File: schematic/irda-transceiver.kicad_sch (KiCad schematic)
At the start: 27 parts, among them J1 Conn_01x03_Pin, J2 Conn_01x03_Pin, J3 Conn_01x03_Pin, J4 Conn_01x03_Pin, J5 Conn_01x03_Pin, J6 Conn_01x03_Pin, J7 Conn_01x06_Pin, U1 MCP2120-I/P, U2 TFDU4101-TT3, Y1 7.3728 MHz

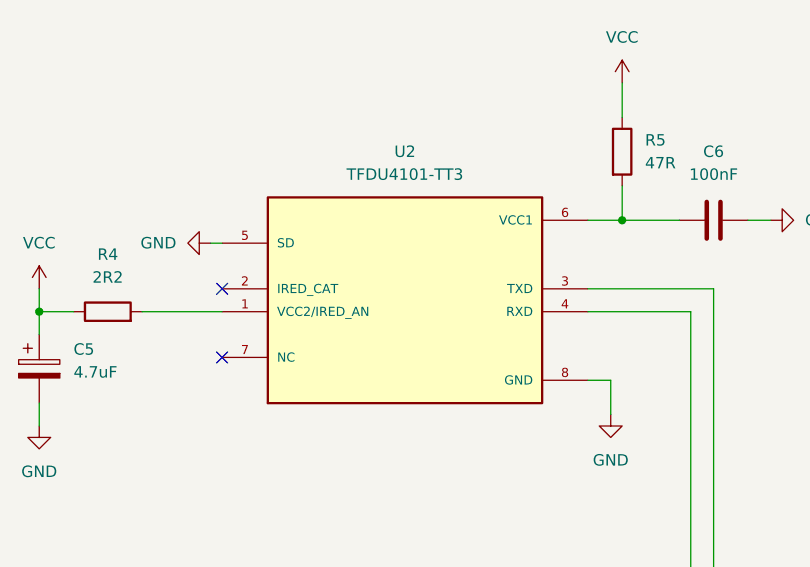
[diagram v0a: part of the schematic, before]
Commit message: TFDU4101 transceiver updated to side view variant (TR3) instead of top view variant (TT3)
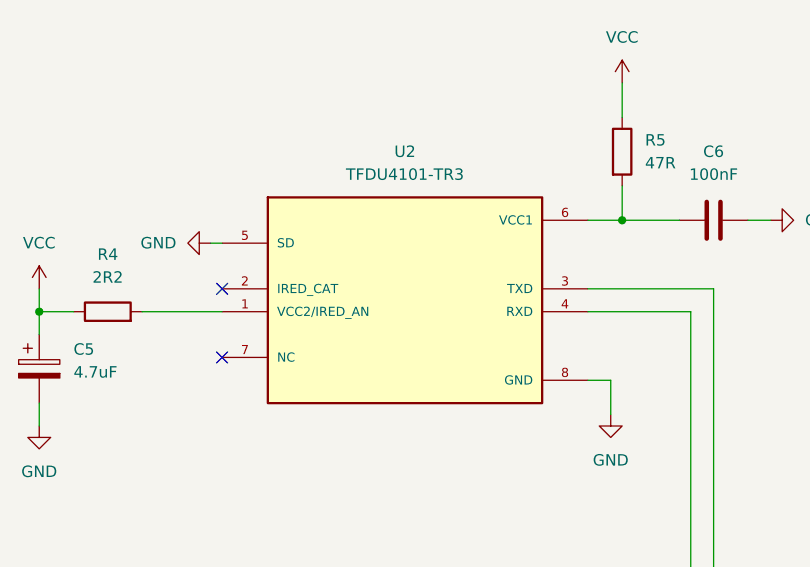
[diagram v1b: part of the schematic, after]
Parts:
- removed U2: TFDU4101-TT3, StockLib:TFDU4101-TT3, symbol StockLib:TFDU4101-TT3
- added U2: TFDU4101-TR3, StockLib:TFDU4101-TR3, symbol StockLib:TFDU4101-TR3
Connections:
- net GND: now also U2.5 (SD), U2.8 (GND)
- net at U1.5 (RXIR): now also U2.4 (RXD)
- net at U1.6 (TXIR): now also U2.3 (TXD)
- net at C6.1, R5.2: now also U2.6 (VCC1)
- net at R4.2: now also U2.1 (VCC2/IRED_AN)
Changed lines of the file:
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@@
-	)
-	(symbol
-		(lib_id "StockLib:TFDU4101-TT3")
-		(at 232.41 57.15 0)
-		(unit 1)
-		(exclude_from_sim no)
-		(in_bom yes)
-		(on_board yes)
-		(dnp no)
-		(fields_autoplaced yes)
-		(property "Reference" "U2"
-			(at 232.41 41.91 0)
-			(effects
-				(font
-					(size 1.27 1.27)
-				)
-			)
-		)
-		(property "Value" "TFDU4101-TT3"
-			(at 232.41 44.45 0)
-			(effects
-				(font
-					(size 1.27 1.27)
-				)
-			)
-		)
-		(property "Footprint" "StockLib:TFDU4101-TT3"
-			(at 232.41 57.15 0)
-			(effects
-				(font
-					(size 1.27 1.27)
-				)
-				(justify bottom)
-				(hide yes)
-			)
-		)
-		(property "Datasheet" ""
-			(at 232.41 57.15 0)
-			(effects
-				(font
-					(size 1.27 1.27)
-				)
-				(hide yes)
-			)
-		)
-		(property "Description" ""
-			(at 232.41 57.15 0)
-			(effects
-				(font
-					(size 1.27 1.27)
-				)
-				(hide yes)
-			)
-		)
-		(property "MF" "Vishay Semiconductor"
-			(at 232.41 57.15 0)
-			(effects
-				(font
-					(size 1.27 1.27)
-				)
-				(justify bottom)
-				(hide yes)
-			)
-		)
-		(property "MAXIMUM_PACKAGE_HEIGHT" "4.7mm"
-			(at 232.41 57.15 0)
-			(effects
-				(font
-					(size 1.27 1.27)
-				)
-				(justify bottom)
-				(hide yes)
-			)
-		)
-		(property "Package" "None"
-			(at 232.41 57.15 0)
-			(effects
-				(font
-					(size 1.27 1.27)
-				)
-				(justify bottom)
-				(hide yes)
-			)
-		)
-		(property "Price" "None"
-			(at 232.41 57.15 0)
-			(effects
-				(font
-					(size 1.27 1.27)
-				)
-				(justify bottom)
-				(hide yes)
-			)
-		)
-		(property "Check_prices" "https://www.snapeda.com/parts/TFDU4101-TT3/Vishay/view-part/?ref=eda"
-			(at 232.41 57.15 0)
-			(effects
-				(font
-					(size 1.27 1.27)
-				)
-				(justify bottom)
-				(hide yes)
-			)
-		)
-		(property "STANDARD" "Manufacturer Recommendations"
-			(at 232.41 57.15 0)
-			(effects
-				(font
-					(size 1.27 1.27)
-				)
-				(justify bottom)
-				(hide yes)
-			)
-		)
-		(property "PARTREV" "2.4"
-			(at 232.41 57.15 0)
-			(effects
-				(font
-					(size 1.27 1.27)
-				)
-				(justify bottom)
-				(hide yes)
-			)
-		)
-		(property "SnapEDA_Link" "https://www.snapeda.com/parts/TFDU4101-TT3/Vishay/view-part/?ref=snap"
-			(at 232.41 57.15 0)
-			(effects
-				(font
-					(size 1.27 1.27)
-				)
-				(justify bottom)
-				(hide yes)
-			)
-		)
-		(property "MP" "TFDU4101-TT3"
-			(at 232.41 57.15 0)
-			(effects
-				(font
-					(size 1.27 1.27)
-				)
-				(justify bottom)
-				(hide yes)
-			)
-		)
-		(property "Description_1" "115.2kbs (SIR) IRDA Transceiver Top View"
-			(at 232.41 57.15 0)
-			(effects
-				(font
-					(size 1.27 1.27)
-				)
-				(justify bottom)
-				(hide yes)
-			)
-		)
-		(property "Availability" "In Stock"
-			(at 232.41 57.15 0)
-			(effects
-				(font
-					(size 1.27 1.27)
-				)
-				(justify bottom)
-				(hide yes)
-			)
-		)
-		(property "MANUFACTURER" "Vishay"
-			(at 232.41 57.15 0)
-			(effects
-				(font
-					(size 1.27 1.27)
-				)
-				(justify bottom)
-				(hide yes)
-			)
-		)
-		(pin "3"
-		)
-		(pin "4"
-		)
-		(pin "5"
-		)
-		(pin "8"
-		)
-		(pin "2"
-		)
-		(pin "6"
-		)
-		(pin "1"
-		)
-		(pin "7"
-		)
-		(instances
-			(project ""
-				(path "/35cc8955-5106-49e3-b197-5188392bf670"
-					(reference "U2")
-					(unit 1)
-				)
-			)
-		)
 	)
 	(symbol
@@
 					(unit 1)
 				)
+			)
+		)
+	)
+	(symbol
+		(lib_id "StockLib:TFDU4101-TR3")
+		(at 232.41 57.15 0)
+		(unit 1)
+		(exclude_from_sim no)
+		(in_bom yes)
+		(on_board yes)
+		(dnp no)
+		(fields_autoplaced yes)
+		(property "Reference" "U2"
+			(at 232.41 41.91 0)
+			(effects
+				(font
+					(size 1.27 1.27)
+				)
+			)
+		)
+		(property "Value" "TFDU4101-TR3"
+			(at 232.41 44.45 0)
+			(effects
+				(font
+					(size 1.27 1.27)
+				)
+			)
+		)
+		(property "Footprint" "StockLib:TFDU4101-TR3"
+			(at 232.41 57.15 0)
+			(effects
+				(font
+					(size 1.27 1.27)
+				)
+				(justify bottom)
+				(hide yes)
+			)
+		)
+		(property "Datasheet" "https://www.vishay.com/docs/81288/tfdu4101.pdf"
+			(at 232.41 57.15 0)
+			(effects
+				(font
+					(size 1.27 1.27)
+				)
+				(hide yes)
+			)
+		)
+		(property "Description" "VISHAY IrDA-Transceiver, 115,2 kb/s, Side View"
+			(at 232.41 57.15 0)
+			(effects
+				(font
+					(size 1.27 1.27)
+				)
+				(hide yes)
+			)
+		)
+		(property "MF" "Vishay Semiconductor"
+			(at 232.41 57.15 0)
+			(effects
+				(font
+					(size 1.27 1.27)
+				)
+				(justify bottom)
+				(hide yes)
+			)
+		)
+		(property "MAXIMUM_PACKAGE_HEIGHT" "4.7mm"
+			(at 232.41 57.15 0)
+			(effects
+				(font
+					(size 1.27 1.27)
+				)
+				(justify bottom)
+				(hide yes)
+			)
+		)
+		(property "Package" "None"
+			(at 232.41 57.15 0)
+			(effects
+				(font
+					(size 1.27 1.27)
+				)
+				(justify bottom)
+				(hide yes)
+			)
+		)
+		(property "Price" "None"
+			(at 232.41 57.15 0)
+			(effects
+				(font
+					(size 1.27 1.27)
+				)
+				(justify bottom)
+				(hide yes)
+			)
+		)
+		(property "Check_prices" "https://www.snapeda.com/parts/TFDU4101-TT3/Vishay/view-part/?ref=eda"
+			(at 232.41 57.15 0)
+			(effects
+				(font
+					(size 1.27 1.27)
+				)
+				(justify bottom)
+				(hide yes)
+			)
+		)
+		(property "STANDARD" "Manufacturer Recommendations"
+			(at 232.41 57.15 0)
+			(effects
+				(font
+					(size 1.27 1.27)
+				)
+				(justify bottom)
+				(hide yes)
+			)
+		)
+		(property "PARTREV" "2.4"
+			(at 232.41 57.15 0)
+			(effects
+				(font
+					(size 1.27 1.27)
+				)
+				(justify bottom)
+				(hide yes)
+			)
+		)
+		(property "SnapEDA_Link" "https://www.snapeda.com/parts/TFDU4101-TT3/Vishay/view-part/?ref=snap"
+			(at 232.41 57.15 0)
+			(effects
+				(font
+					(size 1.27 1.27)
+				)
+				(justify bottom)
+				(hide yes)
+			)
+		)
+		(property "MP" "TFDU4101-TT3"
+			(at 232.41 57.15 0)
+			(effects
+				(font
+					(size 1.27 1.27)
+				)
+				(justify bottom)
+				(hide yes)
+			)
+		)
+		(property "Description_1" "115.2kbs (SIR) IRDA Transceiver Top View"
+			(at 232.41 57.15 0)
+			(effects
+				(font
+					(size 1.27 1.27)
+				)
+				(justify bottom)
+				(hide yes)
+			)
+		)
+		(property "Availability" "In Stock"
+			(at 232.41 57.15 0)
+			(effects
+				(font
+					(size 1.27 1.27)
+				)
+				(justify bottom)
+				(hide yes)
+			)
+		)
+		(property "MANUFACTURER" "Vishay"
+			(at 232.41 57.15 0)
+			(effects
+				(font
+					(size 1.27 1.27)
+				)
+				(justify bottom)
+				(hide yes)
+			)
+		)
+		(pin "6"
+		)
+		(pin "5"
+		)
+		(pin "7"
+		)
+		(pin "4"
+		)
+		(pin "3"
+		)
+		(pin "2"
+		)
+		(pin "8"
+		)
+		(pin "1"
+		)
+		(instances
+			(project ""
+				(path "/35cc8955-5106-49e3-b197-5188392bf670"
+					(reference "U2")
+					(unit 1)
+				)
